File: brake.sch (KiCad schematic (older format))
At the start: 48 parts, among them K1 CONN_3, Q1 PNP, U1 LM555N

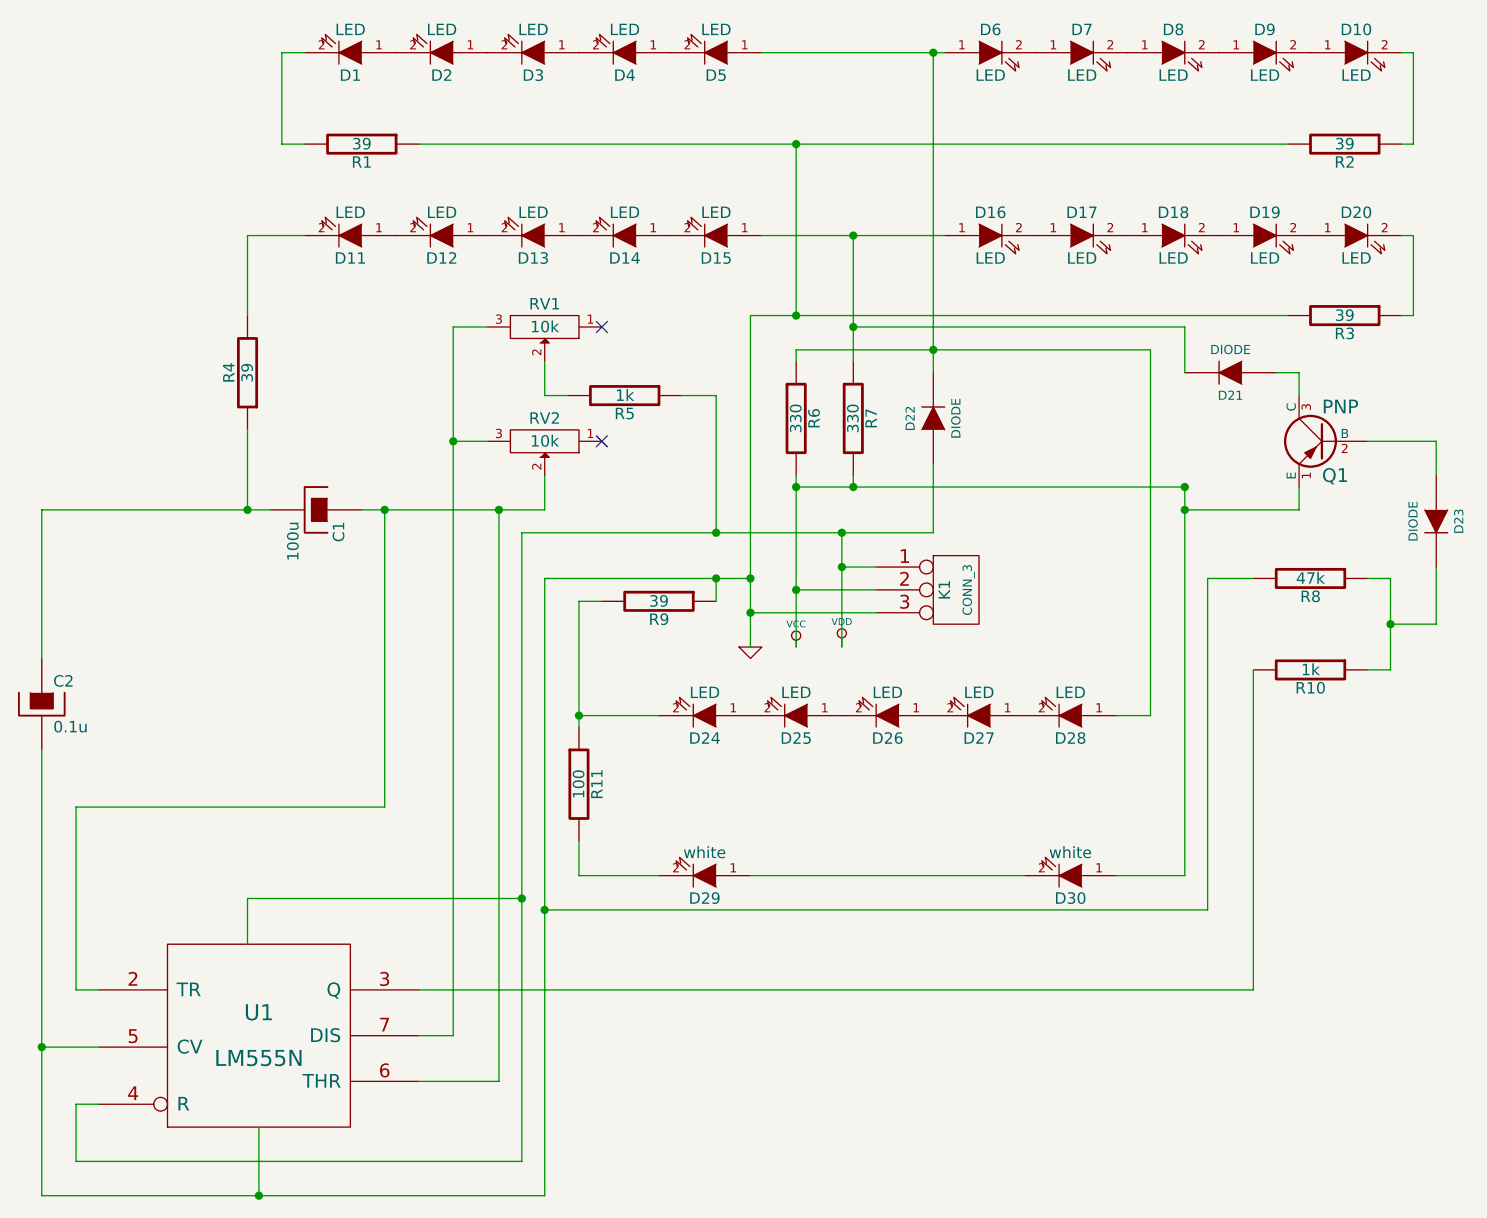
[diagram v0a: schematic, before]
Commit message: began conversion to piranha LEDs
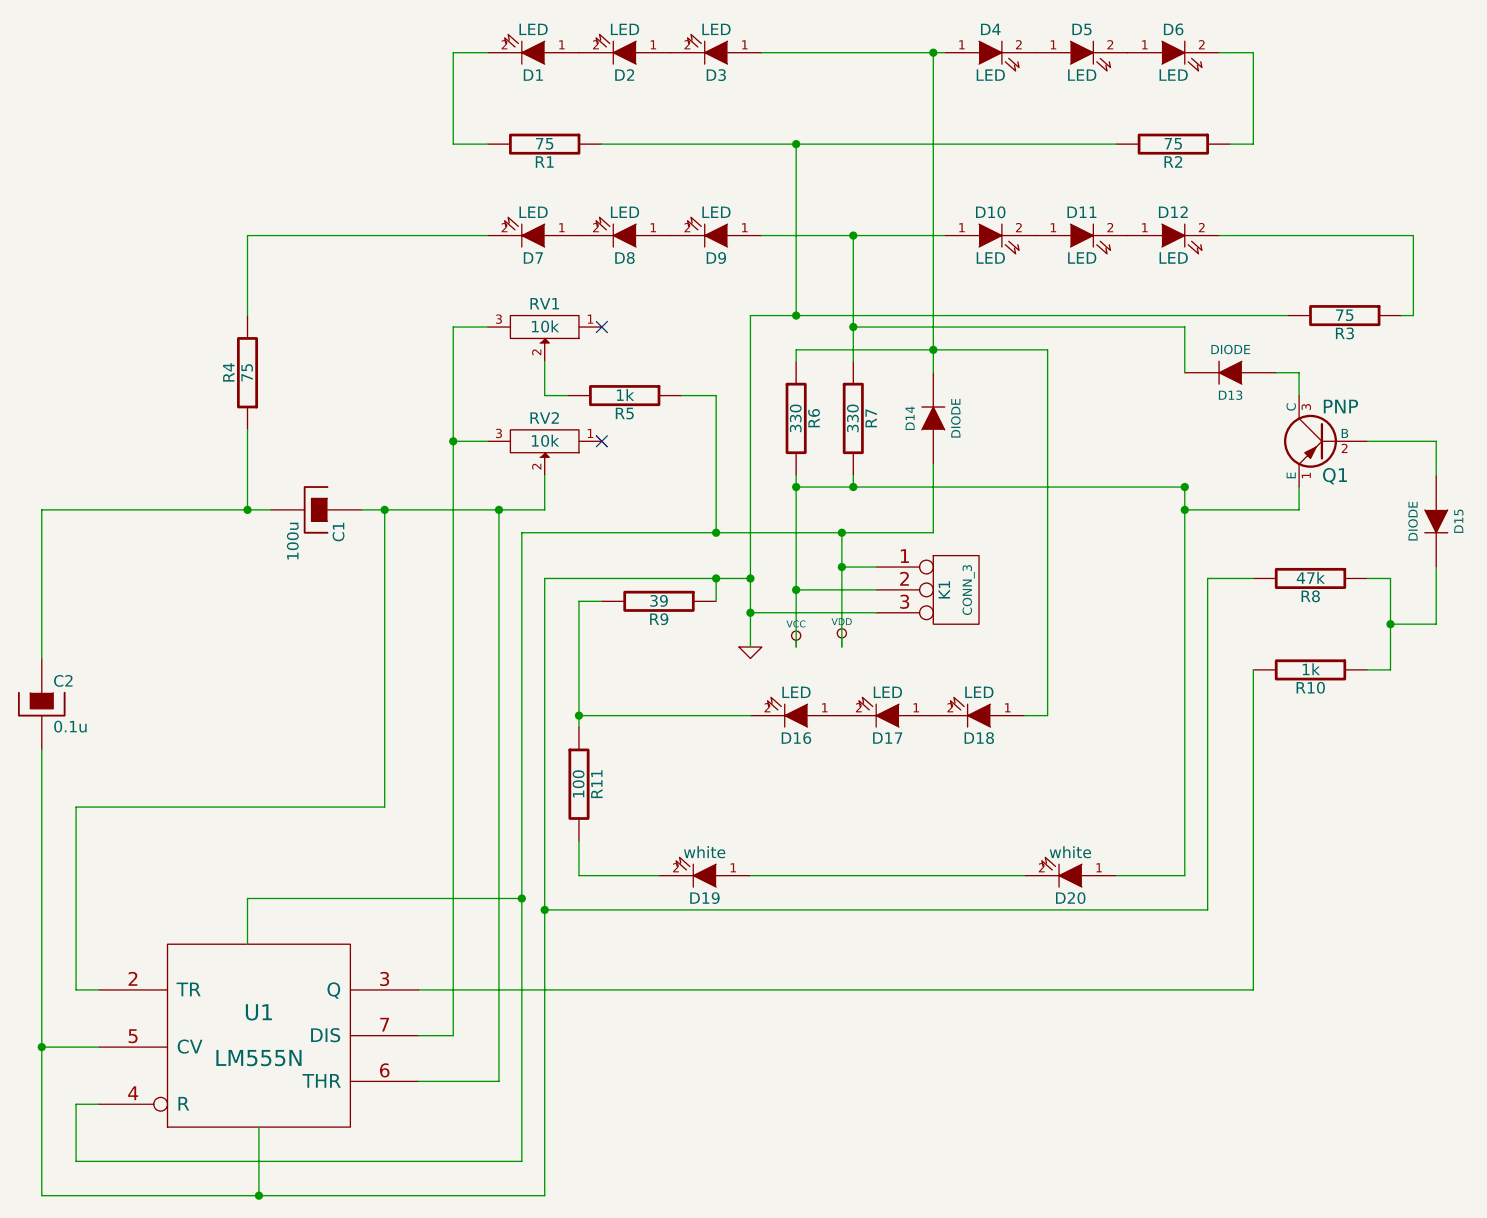
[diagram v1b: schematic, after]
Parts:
- removed D1, D10, D11, D12, D19, D2, D20, D24, D28, D9: LED, symbol LED
- R1, R2, R3, R4: value 39 -> 75
- renumbered D3 to D1, D16 to D10, D17 to D11, D18 to D12, D21 to D13, D22 to D14, D23 to D15, D25 to D16, D26 to D17, D27 to D18, D29 to D19, D4 to D2, D30 to D20, D5 to D3, D6 to D4, D7 to D5, D8 to D6, D13 to D7, D14 to D8, D15 to D9
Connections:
- net at R4.2: now also D7.2 (K)
- net at D14.2 (K), D3.1 (A), D4.1 (A)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: now also D18.1 (A)
- net at D1.2 (K): now also R1.2
- net at R3.1: now also D12.2 (K)
- net at D6.2 (K): now also R2.1
- net at D16.2 (K): now also R11.1, R9.2
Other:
- moved on the sheet: R1, R2
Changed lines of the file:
@@
-EESchema Schematic File Version 2  date Mon 12 Mar 2012 11:23:22 PM MST
+EESchema Schematic File Version 2  date Tue 08 May 2012 11:23:29 PM MST
 LIBS:power
 LIBS:device
@@
 LIBS:contrib
 LIBS:valves
+LIBS:piranha
 LIBS:brake-cache
 EELAYER 25  0
@@
 Sheet 1 1
 Title "Motorcycle tail light"
-Date "13 mar 2012"
+Date "9 may 2012"
 Rev "5"
 Comp "Nate Plamondon"
@@
 $EndDescr
 Wire Wire Line
+	5400 4200 4650 4200
+Wire Wire Line
+	4250 2100 3200 2100
+Wire Wire Line
+	7450 1300 7600 1300
+Wire Wire Line
 	5800 3900 5800 3400
 Connection ~ 5400 3750
@@
 	5400 3900 5400 2450
 Connection ~ 5800 3550
-Wire Wire Line
-	5000 4200 4650 4200
 Wire Wire Line
 	5400 3750 5950 3750
@@
 	5600 1700 5600 2450
 Wire Wire Line
-	7150 4200 7150 2600
+	6700 2600 6700 4200
 Connection ~ 5850 2100
 Wire Wire Line
@@
 	6200 2700 6200 1300
 Wire Wire Line
-	3950 1700 7750 1700
+	4750 1700 7000 1700
 Wire Wire Line
 	5450 2100 6250 2100
@@
 Connection ~ 6200 1300
 Wire Wire Line
-	3450 1300 3350 1300
-Wire Wire Line
-	3350 1300 3350 1700
-Wire Wire Line
-	3350 1700 3450 1700
-Wire Wire Line
-	8250 1300 8300 1300
-Wire Wire Line
-	8300 1300 8300 1700
-Wire Wire Line
-	8300 1700 8250 1700
-Wire Wire Line
-	8250 2100 8300 2100
-Wire Wire Line
-	8300 2100 8300 2450
+	4100 1700 4100 1300
+Wire Wire Line
+	4100 1700 4250 1700
+Wire Wire Line
+	7600 1300 7600 1700
+Wire Wire Line
+	7600 1700 7500 1700
+Wire Wire Line
+	8300 2450 8300 2100
 Wire Wire Line
 	8300 2450 8250 2450
@@
 	5250 3700 5250 3600
 Wire Wire Line
-	7150 4200 7000 4200
-Wire Wire Line
 	5600 2650 5600 2600
 Connection ~ 6200 2600
 Wire Wire Line
-	5600 2600 7150 2600
+	5600 2600 6700 2600
 Wire Wire Line
 	5400 2450 7750 2450
@@
 Connection ~ 3800 3300
 Wire Wire Line
-	3200 2450 3200 2100
-Wire Wire Line
-	3200 2100 3450 2100
+	3200 2100 3200 2450
 Wire Wire Line
 	8200 4000 8200 3600
@@
 	5800 3550 5950 3550
 Wire Wire Line
-	5600 3650 5950 3650
+	5950 3650 5600 3650
 Wire Wire Line
 	4650 4750 4650 4900
@@
 Wire Wire Line
 	5600 3900 5600 3150
-$Comp
-L LED D24
-U 1 1 4F5EC92B
-P 5200 4200
-F 0 "D24" H 5200 4300 50  0000 C CNN
-F 1 "LED" H 5200 4100 50  0000 C CNN
-	1    5200 4200
-	-1   0    0    1
-$EndComp
-$Comp
-L LED D25
+Wire Wire Line
+	8300 2100 7450 2100
+Wire Wire Line
+	4100 1300 4250 1300
+Wire Wire Line
+	6700 4200 6600 4200
+$Comp
+L LED D16
 U 1 1 4F5EC92A
 P 5600 4200
-F 0 "D25" H 5600 4300 50  0000 C CNN
+F 0 "D16" H 5600 4300 50  0000 C CNN
 F 1 "LED" H 5600 4100 50  0000 C CNN
 	1    5600 4200
@@
 $EndComp
 $Comp
-L LED D26
+L LED D17
 U 1 1 4F5EC929
 P 6000 4200
-F 0 "D26" H 6000 4300 50  0000 C CNN
+F 0 "D17" H 6000 4300 50  0000 C CNN
 F 1 "LED" H 6000 4100 50  0000 C CNN
 	1    6000 4200
@@
 $EndComp
 $Comp
-L LED D27
+L LED D18
 U 1 1 4F5EC928
 P 6400 4200
-F 0 "D27" H 6400 4300 50  0000 C CNN
+F 0 "D18" H 6400 4300 50  0000 C CNN
 F 1 "LED" H 6400 4100 50  0000 C CNN
 	1    6400 4200
-	-1   0    0    1
-$EndComp
-$Comp
-L LED D28
-U 1 1 4F5EC927
-P 6800 4200
-F 0 "D28" H 6800 4300 50  0000 C CNN
-F 1 "LED" H 6800 4100 50  0000 C CNN
-	1    6800 4200
 	-1   0    0    1
 $EndComp
@@
 $EndComp
 $Comp
-L DIODE D23
+L DIODE D15
 U 1 1 4F5ED4CD
 P 8400 3350
-F 0 "D23" H 8400 3450 40  0000 C CNN
+F 0 "D15" H 8400 3450 40  0000 C CNN
 F 1 "DIODE" H 8400 3250 40  0000 C CNN
 	1    8400 3350
@@
 $EndComp
 $Comp
-L LED D29
+L LED D19
 U 1 1 4F5EC9FD
 P 5200 4900
-F 0 "D29" H 5200 5000 50  0000 C CNN
+F 0 "D19" H 5200 5000 50  0000 C CNN
 F 1 "white" H 5200 4800 50  0000 C CNN
 	1    5200 4900
@@
 $EndComp
 $Comp
-L LED D30
+L LED D20
 U 1 1 4F5EC9F9
 P 6800 4900
-F 0 "D30" H 6800 5000 50  0000 C CNN
+F 0 "D20" H 6800 5000 50  0000 C CNN
 F 1 "white" H 6800 4800 50  0000 C CNN
 	1    6800 4900
@@
 P 3200 2700
 F 0 "R4" V 3280 2700 50  0000 C CNN
-F 1 "39" V 3200 2700 50  0000 C CNN
+F 1 "75" V 3200 2700 50  0000 C CNN
 	1    3200 2700
 	-1   0    0    1
@@
 L R R1
 U 1 1 4F5EC9CB
-P 3700 1700
-F 0 "R1" V 3780 1700 50  0000 C CNN
-F 1 "39" V 3700 1700 50  0000 C CNN
-	1    3700 1700
+P 4500 1700
+F 0 "R1" V 4580 1700 50  0000 C CNN
+F 1 "75" V 4500 1700 50  0000 C CNN
+	1    4500 1700
 	0    1    1    0
 $EndComp
@@
 L R R2
 U 1 1 4F5EC9C1
-P 8000 1700
-F 0 "R2" V 8080 1700 50  0000 C CNN
-F 1 "39" V 8000 1700 50  0000 C CNN
-	1    8000 1700
+P 7250 1700
+F 0 "R2" V 7330 1700 50  0000 C CNN
+F 1 "75" V 7250 1700 50  0000 C CNN
+	1    7250 1700
 	0    1    1    0
 $EndComp
@@
 P 8000 2450
 F 0 "R3" V 8080 2450 50  0000 C CNN
-F 1 "39" V 8000 2450 50  0000 C CNN
+F 1 "75" V 8000 2450 50  0000 C CNN
 	1    8000 2450
 	0    1    1    0
 $EndComp
 $Comp
-L DIODE D21
+L DIODE D13
 U 1 1 4F5EC9AA
 P 7500 2700
-F 0 "D21" H 7500 2800 40  0000 C CNN
+F 0 "D13" H 7500 2800 40  0000 C CNN
 F 1 "DIODE" H 7500 2600 40  0000 C CNN
 	1    7500 2700
@@
 $EndComp
 $Comp
-L DIODE D22
+L DIODE D14
 U 1 1 4F5EC99C
 P 6200 2900
-F 0 "D22" H 6200 3000 40  0000 C CNN
+F 0 "D14" H 6200 3000 40  0000 C CNN
 F 1 "DIODE" H 6200 2800 40  0000 C CNN
 	1    6200 2900
@@
 $EndComp
 $Comp
-L LED D10
-U 1 1 4F5EC91F
-P 8050 1300
-F 0 "D10" H 8050 1400 50  0000 C CNN
-F 1 "LED" H 8050 1200 50  0000 C CNN
-	1    8050 1300
-	1    0    0    -1
-$EndComp
-$Comp
-L LED D9
-U 1 1 4F5EC91E
-P 7650 1300
-F 0 "D9" H 7650 1400 50  0000 C CNN
-F 1 "LED" H 7650 1200 50  0000 C CNN
-	1    7650 1300
-	1    0    0    -1
-$EndComp
-$Comp
-L LED D8
+L LED D6
 U 1 1 4F5EC91D
 P 7250 1300
-F 0 "D8" H 7250 1400 50  0000 C CNN
+F 0 "D6" H 7250 1400 50  0000 C CNN
 F 1 "LED" H 7250 1200 50  0000 C CNN
 	1    7250 1300
@@
 $EndComp
 $Comp
-L LED D7
+L LED D5
 U 1 1 4F5EC91C
 P 6850 1300
-F 0 "D7" H 6850 1400 50  0000 C CNN
+F 0 "D5" H 6850 1400 50  0000 C CNN
 F 1 "LED" H 6850 1200 50  0000 C CNN
 	1    6850 1300
@@
 $EndComp
 $Comp
-L LED D6
+L LED D4
 U 1 1 4F5EC91B
 P 6450 1300
-F 0 "D6" H 6450 1400 50  0000 C CNN
+F 0 "D4" H 6450 1400 50  0000 C CNN
 F 1 "LED" H 6450 1200 50  0000 C CNN
 	1    6450 1300
@@
 $EndComp
 $Comp
-L LED D16
+L LED D10
 U 1 1 4F5EC91A
 P 6450 2100
-F 0 "D16" H 6450 2200 50  0000 C CNN
+F 0 "D10" H 6450 2200 50  0000 C CNN
 F 1 "LED" H 6450 2000 50  0000 C CNN
 	1    6450 2100
@@
 $EndComp
 $Comp
-L LED D17
+L LED D11
 U 1 1 4F5EC919
 P 6850 2100
-F 0 "D17" H 6850 2200 50  0000 C CNN
+F 0 "D11" H 6850 2200 50  0000 C CNN
 F 1 "LED" H 6850 2000 50  0000 C CNN
 	1    6850 2100
@@
 $EndComp
 $Comp
-L LED D18
+L LED D12
 U 1 1 4F5EC918
 P 7250 2100
-F 0 "D18" H 7250 2200 50  0000 C CNN
+F 0 "D12" H 7250 2200 50  0000 C CNN
 F 1 "LED" H 7250 2000 50  0000 C CNN
 	1    7250 2100
@@
 $EndComp
 $Comp
-L LED D19
-U 1 1 4F5EC917
-P 7650 2100
-F 0 "D19" H 7650 2200 50  0000 C CNN
-F 1 "LED" H 7650 2000 50  0000 C CNN
-	1    7650 2100
-	1    0    0    -1
-$EndComp
-$Comp
-L LED D20
-U 1 1 4F5EC916
-P 8050 2100
-F 0 "D20" H 8050 2200 50  0000 C CNN
-F 1 "LED" H 8050 2000 50  0000 C CNN
-	1    8050 2100
-	1    0    0    -1
-$EndComp
-$Comp
 L LED D1
-U 1 1 4F5EC908
-P 3650 1300
-F 0 "D1" H 3650 1400 50  0000 C CNN
-F 1 "LED" H 3650 1200 50  0000 C CNN
-	1    3650 1300
-	-1   0    0    1
-$EndComp
-$Comp
-L LED D2
-U 1 1 4F5EC907
-P 4050 1300
-F 0 "D2" H 4050 1400 50  0000 C CNN
-F 1 "LED" H 4050 1200 50  0000 C CNN
-	1    4050 1300
-	-1   0    0    1
-$EndComp
-$Comp
-L LED D3
 U 1 1 4F5EC906
 P 4450 1300
-F 0 "D3" H 4450 1400 50  0000 C CNN
+F 0 "D1" H 4450 1400 50  0000 C CNN
 F 1 "LED" H 4450 1200 50  0000 C CNN
 	1    4450 1300
@@
 $EndComp
 $Comp
-L LED D4
+L LED D2
 U 1 1 4F5EC905
 P 4850 1300
-F 0 "D4" H 4850 1400 50  0000 C CNN
+F 0 "D2" H 4850 1400 50  0000 C CNN
 F 1 "LED" H 4850 1200 50  0000 C CNN
 	1    4850 1300
@@
 $EndComp
 $Comp
-L LED D5
+L LED D3
 U 1 1 4F5EC904
 P 5250 1300
-F 0 "D5" H 5250 1400 50  0000 C CNN
+F 0 "D3" H 5250 1400 50  0000 C CNN
 F 1 "LED" H 5250 1200 50  0000 C CNN
 	1    5250 1300
@@
 $EndComp
 $Comp
-L LED D15
+L LED D9
 U 1 1 4F5EC8D1
 P 5250 2100
-F 0 "D15" H 5250 2200 50  0000 C CNN
+F 0 "D9" H 5250 2200 50  0000 C CNN
 F 1 "LED" H 5250 2000 50  0000 C CNN
 	1    5250 2100
@@
 $EndComp
 $Comp
-L LED D14
+L LED D8
 U 1 1 4F5EC8CD
 P 4850 2100
-F 0 "D14" H 4850 2200 50  0000 C CNN
+F 0 "D8" H 4850 2200 50  0000 C CNN
 F 1 "LED" H 4850 2000 50  0000 C CNN
 	1    4850 2100
@@
 $EndComp
 $Comp
-L LED D13
+L LED D7
 U 1 1 4F5EC8BA
 P 4450 2100
-F 0 "D13" H 4450 2200 50  0000 C CNN
+F 0 "D7" H 4450 2200 50  0000 C CNN
 F 1 "LED" H 4450 2000 50  0000 C CNN
 	1    4450 2100
 	-1   0    0    1
 $EndComp
-$Comp
-L LED D12
-U 1 1 4F5EC8B5
-P 4050 2100
-F 0 "D12" H 4050 2200 50  0000 C CNN
-F 1 "LED" H 4050 2000 50  0000 C CNN
-	1    4050 2100
-	-1   0    0    1
-$EndComp
-$Comp
-L LED D11
-U 1 1 4F5EC8A7
-P 3650 2100
-F 0 "D11" H 3650 2200 50  0000 C CNN
-F 1 "LED" H 3650 2000 50  0000 C CNN
-	1    3650 2100
-	-1   0    0    1
-$EndComp
